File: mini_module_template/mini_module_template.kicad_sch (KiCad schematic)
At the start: 0 parts

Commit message: initial design
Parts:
- added D5: D_Schottky, Diode_SMD:D_SMA, symbol Device:D_Schottky
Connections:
- new net +5V: D5.1 (K)
- new net USB/V_BUS: D5.2 (A)
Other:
- added sheet CAN (can.kicad_sch)
- added sheet MCU (MCU.kicad_sch)
- added sheet POWER (POWER.kicad_sch)
- added sheet STLINK (STLINK.kicad_sch)
- added sheet USB (usb.kicad_sch)
- title: (none) -> Root schematic

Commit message: Leyout rev 1
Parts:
- removed D5: D_Schottky, Diode_SMD:D_SMA, symbol Device:D_Schottky
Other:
- added sheet user-schematic (user-schematic.kicad_sch)
- sheet USB ports: added none; removed V_BUS
- note added: "<-------"
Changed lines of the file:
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@@
-	(wire
-		(pts
-			(xy 198.12 45.72) (xy 204.47 45.72)
-		)
-		(stroke
-			(width 0)
-			(type default)
-		)
-	)
 	(wire
 		(pts
@@
 	(wire
 		(pts
-			(xy 214.63 45.72) (xy 214.63 43.18)
-		)
-		(stroke
-			(width 0)
-			(type default)
-		)
-	)
-	(wire
-		(pts
 			(xy 157.48 53.34) (xy 161.29 53.34)
 		)
@@
 	(wire
 		(pts
-			(xy 212.09 45.72) (xy 214.63 45.72)
-		)
-		(stroke
-			(width 0)
-			(type default)
-		)
-	)
-	(wire
-		(pts
 			(xy 154.94 50.8) (xy 154.94 67.31)
 		)
@@
 		)
 	)
-	(symbol
-		(lib_id "power:+5V")
-		(at 214.63 43.18 0)
-		(mirror y)
-		(unit 1)
+	(text "<-------\n"
 		(exclude_from_sim no)
-		(in_bom yes)
-		(on_board yes)
-		(dnp no)
-		(property "Reference" "#PWR030"
-			(at 214.63 46.99 0)
-			(effects
-				(font
-					(size 1.27 1.27)
-				)
-				(hide yes)
-			)
-		)
-		(property "Value" "+5V"
-			(at 214.63 39.37 0)
-			(effects
-				(font
-					(size 1.27 1.27)
-				)
-			)
-		)
-		(property "Footprint" ""
-			(at 214.63 43.18 0)
-			(effects
-				(font
-					(size 1.27 1.27)
-				)
-				(hide yes)
-			)
-		)
-		(property "Datasheet" ""
-			(at 214.63 43.18 0)
-			(effects
-				(font
-					(size 1.27 1.27)
-				)
-				(hide yes)
-			)
-		)
-		(property "Description" ""
-			(at 214.63 43.18 0)
-			(effects
-				(font
-					(size 1.27 1.27)
-				)
-				(hide yes)
-			)
-		)
-		(pin "1"
-		)
-		(instances
-			(project "mini_module_template"
-				(path "/f131027f-631c-4099-b0ec-5f883860005f"
-					(reference "#PWR030")
-					(unit 1)
-				)
-			)
-		)
-	)
-	(symbol
-		(lib_id "Device:D_Schottky")
-		(at 208.28 45.72 180)
-		(unit 1)
-		(exclude_from_sim no)
-		(in_bom yes)
-		(on_board yes)
-		(dnp no)
-		(property "Reference" "D5"
-			(at 208.28 48.26 0)
-			(effects
-				(font
-					(size 1.27 1.27)
-				)
-			)
-		)
-		(property "Value" "D_Schottky"
-			(at 208.28 43.18 0)
-			(effects
-				(font
-					(size 1.27 1.27)
-				)
-			)
-		)
-		(property "Footprint" "Diode_SMD:D_SMA"
-			(at 208.28 45.72 0)
-			(effects
-				(font
-					(size 1.27 1.27)
-				)
-				(hide yes)
-			)
-		)
-		(property "Datasheet" "~"
-			(at 208.28 45.72 0)
-			(effects
-				(font
-					(size 1.27 1.27)
-				)
-				(hide yes)
-			)
-		)
-		(property "Description" ""
-			(at 208.28 45.72 0)
-			(effects
-				(font
-					(size 1.27 1.27)
-				)
-				(hide yes)
-			)
-		)
-		(pin "1"
-		)
-		(pin "2"
-		)
-		(instances
-			(project "mini_module_template"
-				(path "/f131027f-631c-4099-b0ec-5f883860005f"
-					(reference "D5")
-					(unit 1)
-				)
+		(at 83.058 75.184 0)
+		(effects
+			(font
+				(size 1.27 1.27)
 			)
 		)
@@
 				)
 				(justify left top)
-			)
-		)
-		(pin "V_BUS" output
-			(at 198.12 45.72 0)
-			(effects
-				(font
-					(size 1.27 1.27)
-				)
-				(justify right)
 			)
 		)
@@
 				)
 			)
+		)
+	)
+	(sheet
+		(at 39.37 53.34)
+		(size 34.29 44.45)
+		(fields_autoplaced yes)
+		(stroke
+			(width 0.1524)
+			(type solid)
+		)
+		(fill
+			(color 0 0 0 0.0000)
+		)
+		(property "Sheetname" "user-schematic"
+			(at 39.37 52.6284 0)
+			(effects
+				(font
+					(size 1.27 1.27)
+				)
+				(justify left bottom)
+			)
+		)
+		(property "Sheetfile" "user-schematic.kicad_sch"
+			(at 39.37 98.3746 0)
+			(effects
+				(font
+					(size 1.27 1.27)
+				)
+				(justify left top)
+			)
+		)
+		(instances
+			(project "mini_module_template"
+				(path "/f131027f-631c-4099-b0ec-5f883860005f"
+					(page "7")
+				)
+			)

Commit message: addded crystal to usb hub. added connection tabs to stm+stlink
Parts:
- added JP1, JP2, JP3: SolderJumper_2_Bridged, Jumper:SolderJumper-2_P1.3mm_Open_RoundedPad1.0x1.5mm, symbol Jumper:SolderJumper_2_Bridged
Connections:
- net MCU/NRST: now also JP3.1 (A)
- net MCU/SWCLK: now also JP1.1 (A)
- net MCU/SWDIO: now also JP2.1 (A)
- new net STLINK/NRST: JP3.2 (B)
- new net STLINK/SWCLK: JP1.2 (B)
- new net STLINK/SWDIO: JP2.2 (B)
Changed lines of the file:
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@@
+	(wire
+		(pts
+			(xy 149.86 77.47) (xy 161.29 77.47)
+		)
+		(stroke
+			(width 0)
+			(type default)
+		)
+	)
 	(wire
 		(pts
@@
 	(wire
 		(pts
-			(xy 130.81 74.93) (xy 161.29 74.93)
-		)
-		(stroke
-			(width 0)
-			(type default)
-		)
-	)
-	(wire
-		(pts
 			(xy 130.81 106.68) (xy 161.29 106.68)
 		)
@@
 	(wire
 		(pts
+			(xy 149.86 80.01) (xy 161.29 80.01)
+		)
+		(stroke
+			(width 0)
+			(type default)
+		)
+	)
+	(wire
+		(pts
 			(xy 161.29 64.77) (xy 157.48 64.77)
 		)
@@
 	(wire
 		(pts
-			(xy 130.81 80.01) (xy 161.29 80.01)
+			(xy 130.81 77.47) (xy 142.24 77.47)
 		)
 		(stroke
@@
 	(wire
 		(pts
-			(xy 130.81 77.47) (xy 161.29 77.47)
+			(xy 130.81 74.93) (xy 142.24 74.93)
+		)
+		(stroke
+			(width 0)
+			(type default)
+		)
+	)
+	(wire
+		(pts
+			(xy 149.86 74.93) (xy 161.29 74.93)
 		)
 		(stroke
@@
 		(pts
 			(xy 130.81 119.38) (xy 139.7 119.38)
+		)
+		(stroke
+			(width 0)
+			(type default)
+		)
+	)
+	(wire
+		(pts
+			(xy 130.81 80.01) (xy 142.24 80.01)
 		)
 		(stroke
@@
 			)
 		)
+	)
+	(symbol
+		(lib_id "Jumper:SolderJumper_2_Bridged")
+		(at 146.05 80.01 0)
+		(unit 1)
+		(exclude_from_sim yes)
+		(in_bom no)
+		(on_board yes)
+		(dnp no)
+		(property "Reference" "JP3"
+			(at 143.256 81.534 0)
+			(effects
+				(font
+					(size 1.27 1.27)
+				)
+			)
+		)
+		(property "Value" "SolderJumper_2_Bridged"
+			(at 146.05 76.2 0)
+			(effects
+				(font
+					(size 1.27 1.27)
+				)
+				(hide yes)
+			)
+		)
+		(property "Footprint" "Jumper:SolderJumper-2_P1.3mm_Open_RoundedPad1.0x1.5mm"
+			(at 146.05 80.01 0)
+			(effects
+				(font
+					(size 1.27 1.27)
+				)
+				(hide yes)
+			)
+		)
+		(property "Datasheet" "~"
+			(at 146.05 80.01 0)
+			(effects
+				(font
+					(size 1.27 1.27)
+				)
+				(hide yes)
+			)
+		)
+		(property "Description" "Solder Jumper, 2-pole, closed/bridged"
+			(at 146.05 80.01 0)
+			(effects
+				(font
+					(size 1.27 1.27)
+				)
+				(hide yes)
+			)
+		)
+		(pin "2"
+		)
+		(pin "1"
+		)
+		(instances
+			(project "mini_module_template"
+				(path "/f131027f-631c-4099-b0ec-5f883860005f"
+					(reference "JP3")
+					(unit 1)
+				)
+			)
+		)
+	)
+	(symbol
+		(lib_id "Jumper:SolderJumper_2_Bridged")
+		(at 146.05 77.47 0)
+		(unit 1)
+		(exclude_from_sim yes)
+		(in_bom no)
+		(on_board yes)
+		(dnp no)
+		(property "Reference" "JP2"
+			(at 143.002 78.74 0)
+			(effects
+				(font
+					(size 1.27 1.27)
+				)
+			)
+		)
+		(property "Value" "SolderJumper_2_Bridged"
+			(at 146.05 73.66 0)
+			(effects
+				(font
+					(size 1.27 1.27)
+				)
+				(hide yes)
+			)
+		)
+		(property "Footprint" "Jumper:SolderJumper-2_P1.3mm_Open_RoundedPad1.0x1.5mm"
+			(at 146.05 77.47 0)
+			(effects
+				(font
+					(size 1.27 1.27)
+				)
+				(hide yes)
+			)
+		)
+		(property "Datasheet" "~"
+			(at 146.05 77.47 0)
+			(effects
+				(font
+					(size 1.27 1.27)
+				)
+				(hide yes)
+			)
+		)
+		(property "Description" "Solder Jumper, 2-pole, closed/bridged"
+			(at 146.05 77.47 0)
+			(effects
+				(font
+					(size 1.27 1.27)
+				)
+				(hide yes)
+			)
+		)
+		(pin "2"
+		)
+		(pin "1"
+		)
+		(instances
+			(project "mini_module_template"
+				(path "/f131027f-631c-4099-b0ec-5f883860005f"
+					(reference "JP2")
+					(unit 1)
+				)
+			)
+		)
+	)
+	(symbol
+		(lib_id "Jumper:SolderJumper_2_Bridged")
+		(at 146.05 74.93 0)
+		(unit 1)
+		(exclude_from_sim yes)
+		(in_bom no)
+		(on_board yes)
+		(dnp no)
+		(property "Reference" "JP1"
+			(at 143.002 73.914 0)
+			(effects
+				(font
+					(size 1.27 1.27)
+				)
+			)
+		)
+		(property "Value" "SolderJumper_2_Bridged"
+			(at 146.05 71.12 0)
+			(effects
+				(font
+					(size 1.27 1.27)
+				)
+				(hide yes)
+			)
+		)
+		(property "Footprint" "Jumper:SolderJumper-2_P1.3mm_Open_RoundedPad1.0x1.5mm"
+			(at 146.05 74.93 0)
+			(effects
+				(font
+					(size 1.27 1.27)
+				)
+				(hide yes)
+			)
+		)
+		(property "Datasheet" "~"
+			(at 146.05 74.93 0)
+			(effects
+				(font
+					(size 1.27 1.27)
+				)
+				(hide yes)
+			)
+		)
+		(property "Description" "Solder Jumper, 2-pole, closed/bridged"
+			(at 146.05 74.93 0)
+			(effects
+				(font
+					(size 1.27 1.27)
+				)
+				(hide yes)
+			)
+		)
+		(pin "2"
+		)
+		(pin "1"
+		)
+		(instances
+			(project ""
+				(path "/f131027f-631c-4099-b0ec-5f883860005f"
+					(reference "JP1")
+					(unit 1)
+				)
+			)
+		)

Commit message: fixed can and usb traces
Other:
- sheet CAN ports: added CAN+, CAN-; removed CAN_H, CAN_L
- sheet POWER ports: added CAN+, CAN-; removed CAN_H, CAN_L
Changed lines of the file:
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@@
 			)
 		)
-		(pin "CAN_H" input
+		(pin "CAN+" input
 			(at 153.67 135.89 90)
 			(effects
@@
 			)
 		)
-		(pin "CAN_L" input
+		(pin "CAN-" input
 			(at 156.21 135.89 90)
 			(effects
@@
 			)
 		)
-		(pin "CAN_H" input
+		(pin "CAN+" input
 			(at 161.29 118.11 180)
 			(effects
@@
 			)
 		)
-		(pin "CAN_L" input
+		(pin "CAN-" input
 			(at 161.29 120.65 180)
 			(effects

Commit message: rev 1.0 finished
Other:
- sheet POWER ports: added USB_DOWNSTREAM_D+, USB_DOWNSTREAM_D-, USB_UPSTREAM_D+, USB_UPSTREAM_D-; removed none
- sheet USB ports: added USB_DOWNSTREM_D+, USB_DOWNSTREM_D-, USB_SWITCH_D+, USB_SWITCH_D-; removed none
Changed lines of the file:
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@@
+	(wire
+		(pts
+			(xy 203.2 46.99) (xy 198.12 46.99)
+		)
+		(stroke
+			(width 0)
+			(type default)
+		)
+	)
+	(wire
+		(pts
+			(xy 165.1 148.59) (xy 203.2 148.59)
+		)
+		(stroke
+			(width 0)
+			(type default)
+		)
+	)
 	(wire
 		(pts
@@
 	(wire
 		(pts
+			(xy 165.1 156.21) (xy 208.28 156.21)
+		)
+		(stroke
+			(width 0)
+			(type default)
+		)
+	)
+	(wire
+		(pts
 			(xy 161.29 67.31) (xy 154.94 67.31)
 		)
@@
 	(wire
 		(pts
+			(xy 200.66 146.05) (xy 200.66 49.53)
+		)
+		(stroke
+			(width 0)
+			(type default)
+		)
+	)
+	(wire
+		(pts
 			(xy 156.21 120.65) (xy 156.21 135.89)
 		)
@@
 	(wire
 		(pts
+			(xy 205.74 153.67) (xy 205.74 36.83)
+		)
+		(stroke
+			(width 0)
+			(type default)
+		)
+	)
+	(wire
+		(pts
 			(xy 130.81 104.14) (xy 161.29 104.14)
 		)
@@
 	(wire
 		(pts
+			(xy 198.12 36.83) (xy 205.74 36.83)
+		)
+		(stroke
+			(width 0)
+			(type default)
+		)
+	)
+	(wire
+		(pts
 			(xy 154.94 50.8) (xy 161.29 50.8)
 		)
@@
 	(wire
 		(pts
+			(xy 198.12 34.29) (xy 208.28 34.29)
+		)
+		(stroke
+			(width 0)
+			(type default)
+		)
+	)
+	(wire
+		(pts
 			(xy 161.29 64.77) (xy 157.48 64.77)
 		)
@@
 	(wire
 		(pts
+			(xy 165.1 153.67) (xy 205.74 153.67)
+		)
+		(stroke
+			(width 0)
+			(type default)
+		)
+	)
+	(wire
+		(pts
 			(xy 157.48 64.77) (xy 157.48 53.34)
 		)
@@
 	(wire
 		(pts
+			(xy 165.1 146.05) (xy 200.66 146.05)
+		)
+		(stroke
+			(width 0)
+			(type default)
+		)
+	)
+	(wire
+		(pts
 			(xy 152.4 48.26) (xy 161.29 48.26)
 		)
@@
 	(wire
 		(pts
+			(xy 208.28 156.21) (xy 208.28 34.29)
+		)
+		(stroke
+			(width 0)
+			(type default)
+		)
+	)
+	(wire
+		(pts
+			(xy 198.12 49.53) (xy 200.66 49.53)
+		)
+		(stroke
+			(width 0)
+			(type default)
+		)
+	)
+	(wire
+		(pts
 			(xy 157.48 53.34) (xy 161.29 53.34)
 		)
@@
 		(pts
 			(xy 149.86 74.93) (xy 161.29 74.93)
+		)
+		(stroke
+			(width 0)
+			(type default)
+		)
+	)
+	(wire
+		(pts
+			(xy 203.2 148.59) (xy 203.2 46.99)
 		)
 		(stroke
@@
 			)
 		)
+		(pin "USB_SWITCH_D-" bidirectional
+			(at 198.12 36.83 0)
+			(effects
+				(font
+					(size 1.27 1.27)
+				)
+				(justify right)
+			)
+		)
+		(pin "USB_SWITCH_D+" input
+			(at 198.12 34.29 0)
+			(effects
+				(font
+					(size 1.27 1.27)
+				)
+				(justify right)
+			)
+		)
+		(pin "USB_DOWNSTREM_D-" bidirectional
+			(at 198.12 49.53 0)
+			(effects
+				(font
+					(size 1.27 1.27)
+				)
+				(justify right)
+			)
+		)
+		(pin "USB_DOWNSTREM_D+" input
+			(at 198.12 46.99 0)
+			(effects
+				(font
+					(size 1.27 1.27)
+				)
+				(justify right)
+			)
+		)
 		(instances
 			(project "mini_module_template"
@@
 			(effects
 				(font
+					(size 1.27 1.27)
+				)
+				(justify right)
+			)
+		)
+		(pin "USB_UPSTREAM_D+" input
+			(at 165.1 156.21 0)
+			(effects
+				(font
+					(size 1.27 1.27)
+				)
+				(justify right)
+			)
+		)
+		(pin "USB_UPSTREAM_D-" input
+			(at 165.1 153.67 0)
+			(effects
+				(font
+					(size 1.27 1.27)
+				)
+				(justify right)
+			)
+		)
+		(pin "USB_DOWNSTREAM_D+" input
+			(at 165.1 148.59 0)
+			(effects
+				(font
+					(size 1.27 1.27)
+				)
+				(justify right)
+			)
+		)
+		(pin "USB_DOWNSTREAM_D-" input
+			(at 165.1 146.05 0)
+			(effects
+				(font

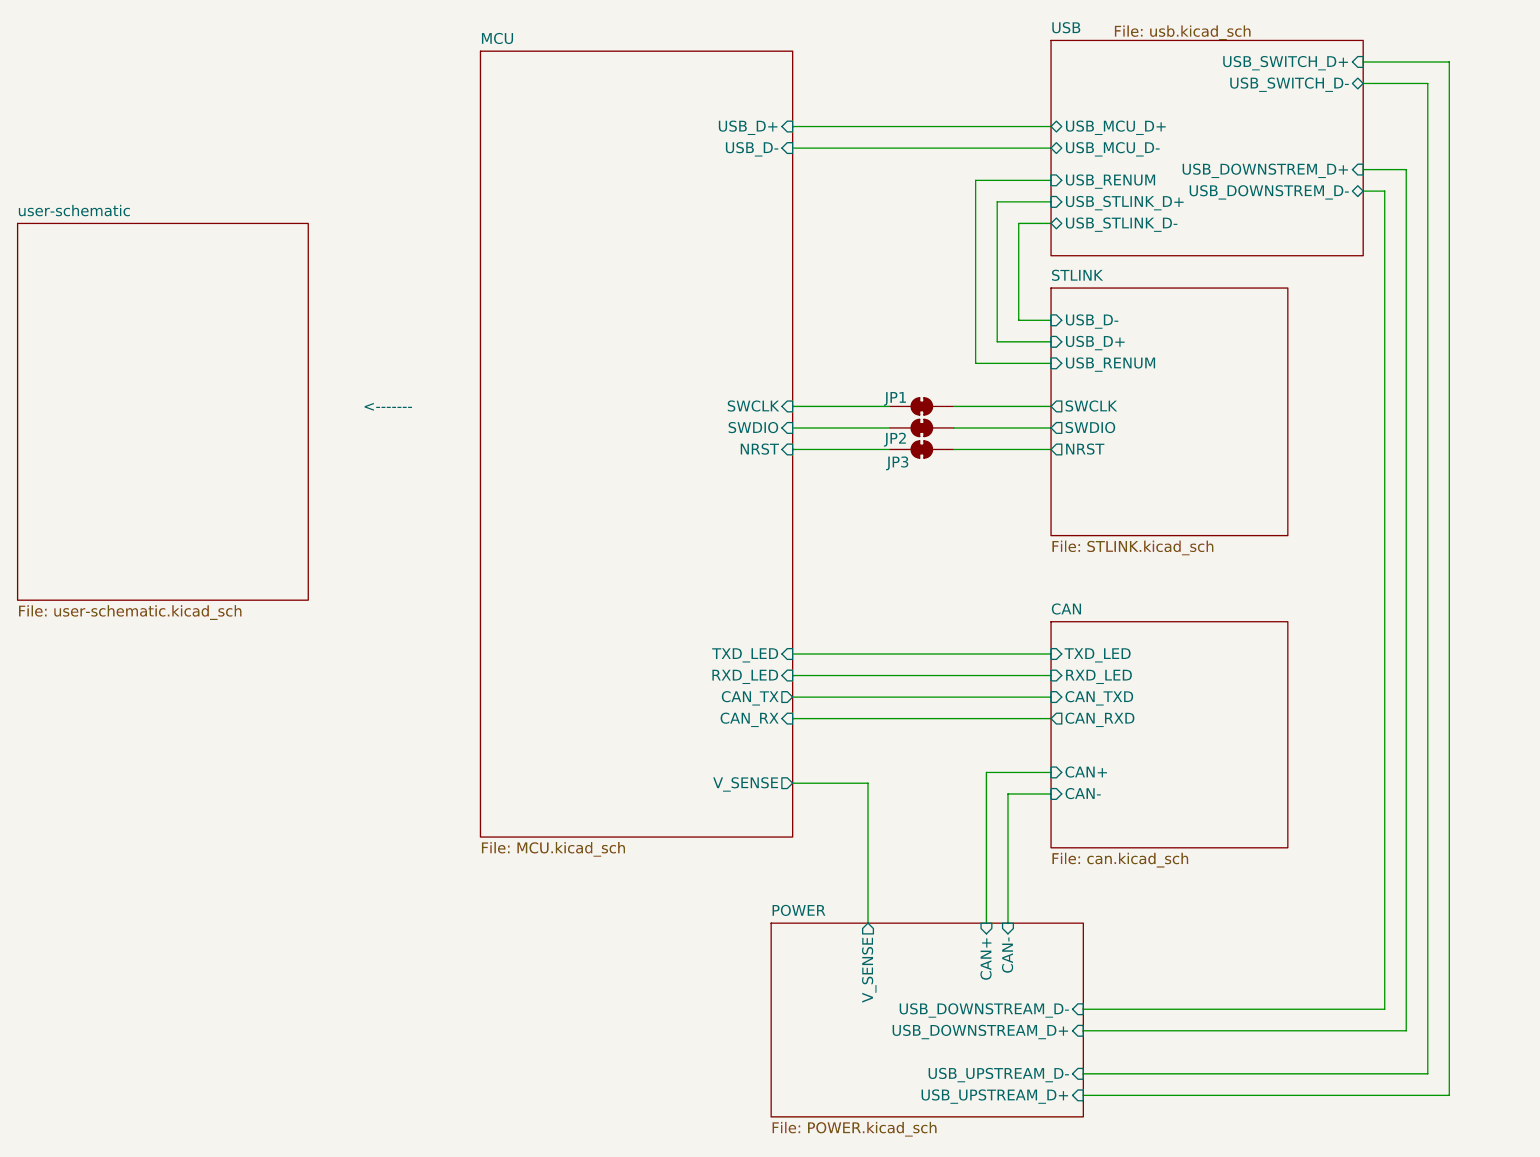
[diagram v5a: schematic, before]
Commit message: revison C, aded 2 can support and gight voltage input stepdown
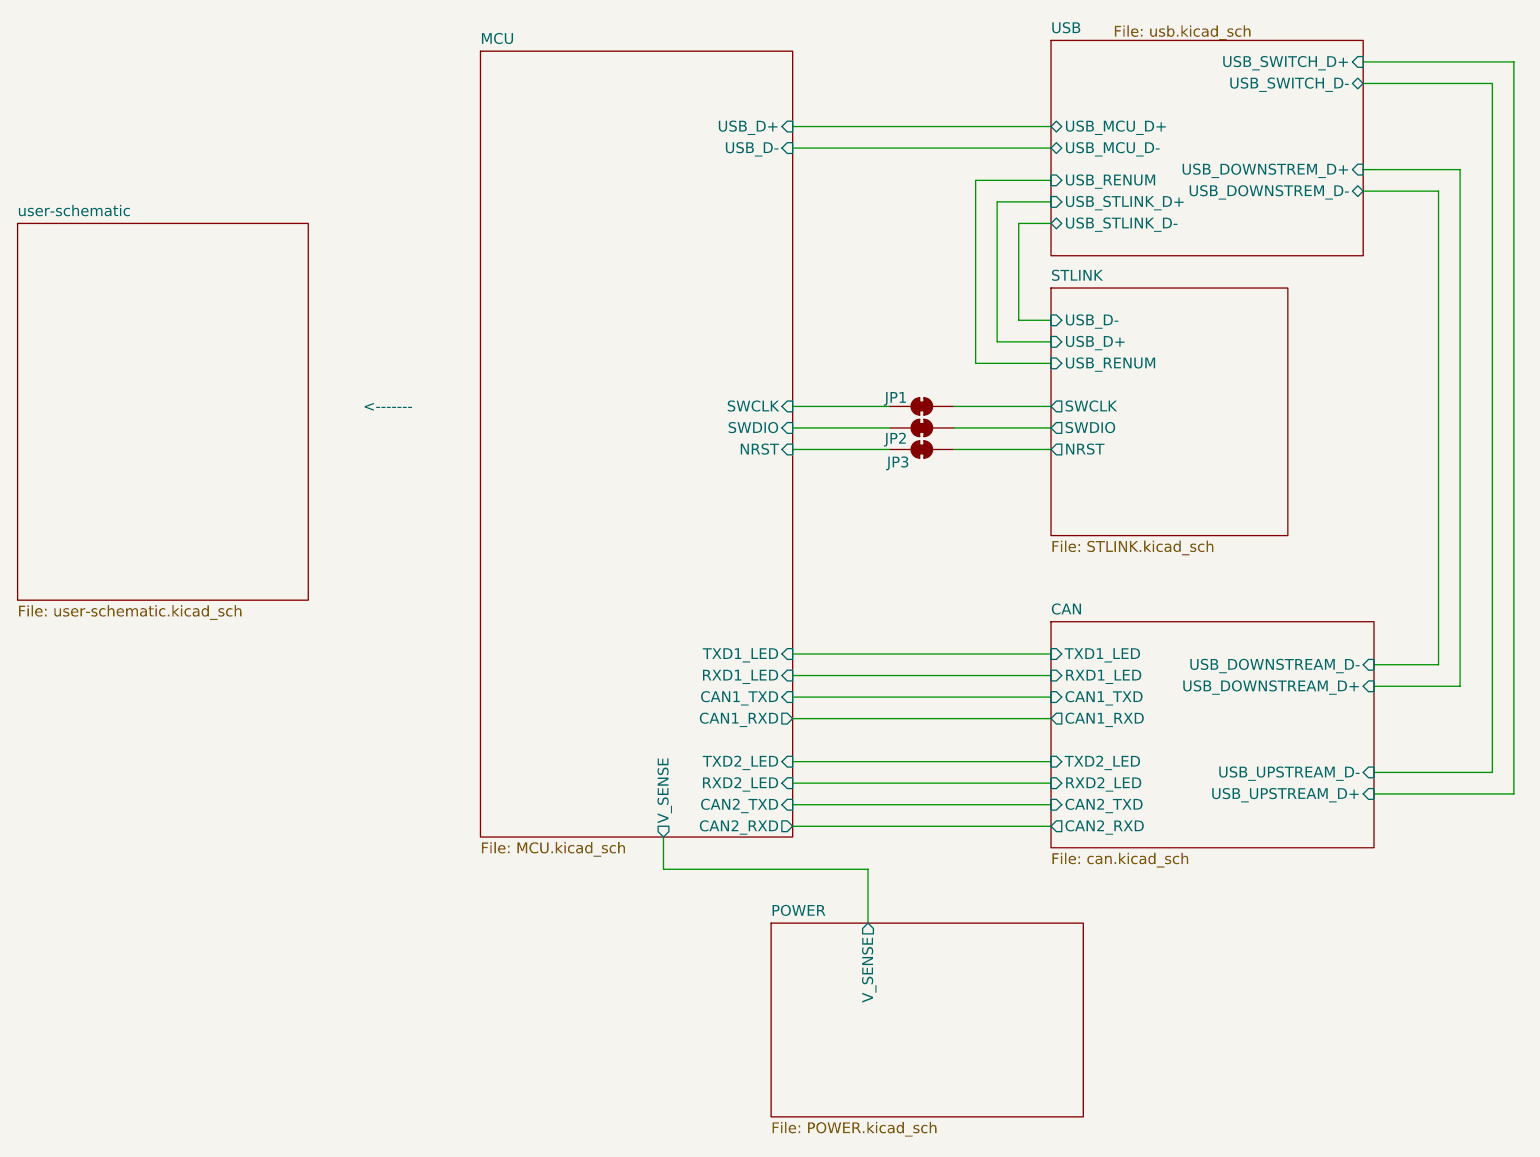
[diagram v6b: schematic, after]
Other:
- sheet CAN ports: added CAN1_RXD, CAN1_TXD, CAN2_RXD, CAN2_TXD, RXD1_LED, RXD2_LED, TXD1_LED, TXD2_LED, USB_DOWNSTREAM_D+, USB_DOWNSTREAM_D-, USB_UPSTREAM_D+, USB_UPSTREAM_D-; removed CAN+, CAN-, CAN_RXD, CAN_TXD, RXD_LED, TXD_LED
- sheet MCU ports: added CAN1_RXD, CAN1_TXD, CAN2_RXD, CAN2_TXD, RXD1_LED, RXD2_LED, TXD1_LED, TXD2_LED; removed CAN_RX, CAN_TX, RXD_LED, TXD_LED
- sheet POWER ports: added none; removed CAN+, CAN-, USB_DOWNSTREAM_D+, USB_DOWNSTREAM_D-, USB_UPSTREAM_D+, USB_UPSTREAM_D-

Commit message: updaet schematic
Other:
- company: (none) -> Patryk Dudziński
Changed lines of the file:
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@@
 	(title_block
 		(title "Root schematic")
+		(date "2025-01-10")
+		(rev "1.0")
+		(company "Patryk Dudziński")
 	)
 	(wire
